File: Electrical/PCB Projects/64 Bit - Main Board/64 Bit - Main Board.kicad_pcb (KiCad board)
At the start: 4 copper layers, 200 x 100 mm, 238 parts, among them J1 61301021821, J10 M20-7920242R, J11 M20-7920242R, J12 M20-7920242R, J13 M20-7920242R, J14 1985195, J15 Conn_01x09, J16 Conn_01x09, J17 M20-7920242R, J18 M20-7920242R, J2 61301021821, J3 61301021821, J4 M20-7920242R, J5 USBC, J6 M20-7920242R, J7 PJ-102A, J8 M20-7920242R, J9 M20-7920242R, K1 JS-12N-K, K2 JS-12N-K, K3 JS-12N-K, K4 PR30-5V-450-1A-E, K5 PR30-12V-450-1A-E, P1 Conn_01x02, Q1 2N7002, Q10 XP231P0201TR-G, Q11 2N7002, Q2 XP231P0201TR-G, Q3 2N7002, Q4 2N7002, Q5 2N7002, Q6 XP231P0201TR-G, Q7 XP231P0201TR-G, Q8 2N7002, Q9 2N7002, SW1 1985195, SW2 1985195, SW3 1985195, SW4 1985195, SW5 L102011MS02Q, SW6 power_switch, U1 STM32F446RETx, U10 VEML7700-TR, U2 PCA9306, U3 DS1307+, U4 74HC3G34DC, U5 74HC3G34DC, U6 74HC3G34DC, U7 EN12-VS20AF20, U8 24LC64, U9 ESP32-C6-LCD-1.47, Y1 Crystal_GND24, Y2 32.768kHz-12.6pF, Y3 32.768kHz-12.6pF

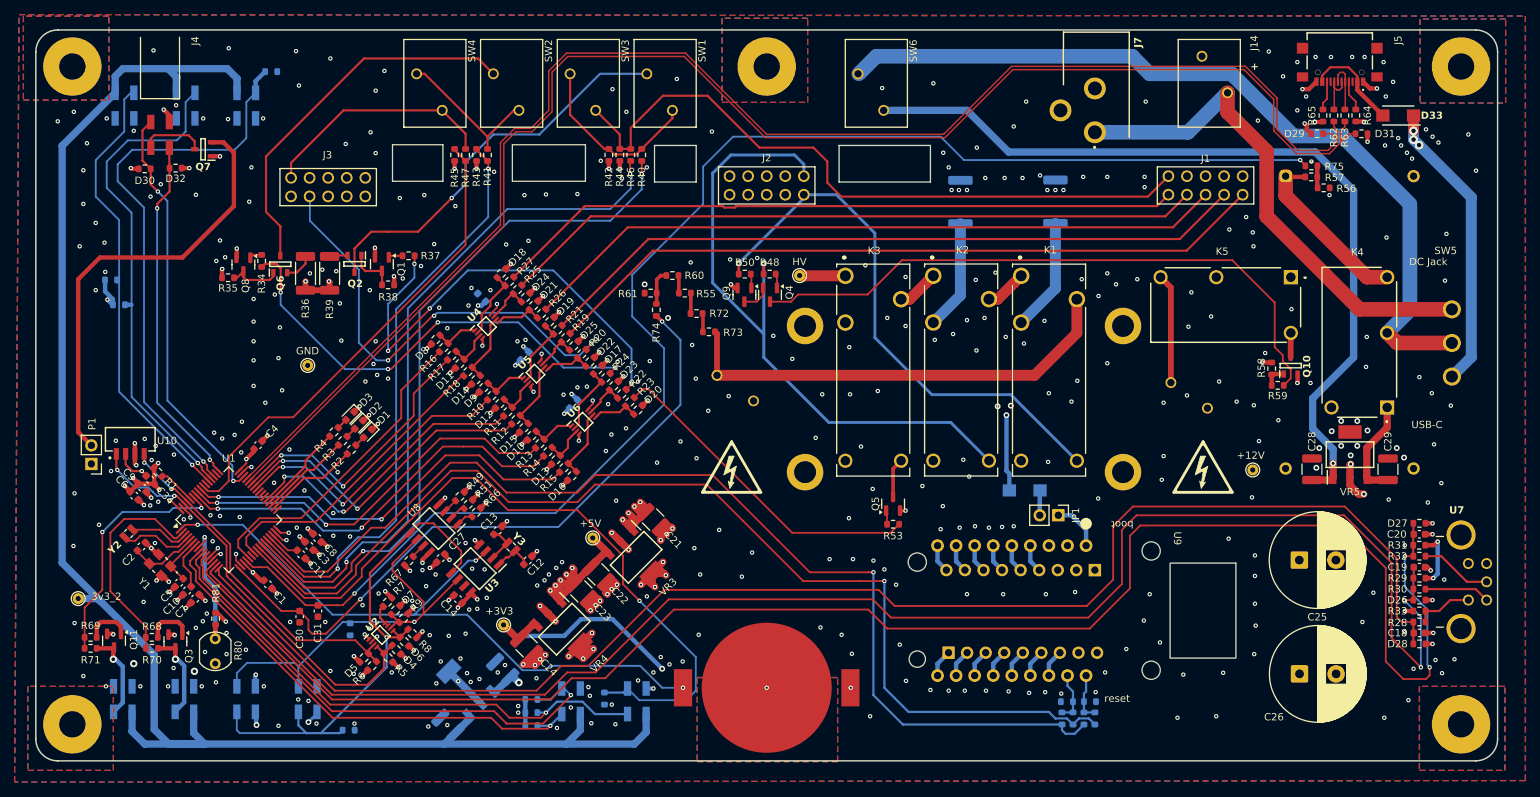
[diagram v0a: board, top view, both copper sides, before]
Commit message: near final state. Includes BOM, price, etc
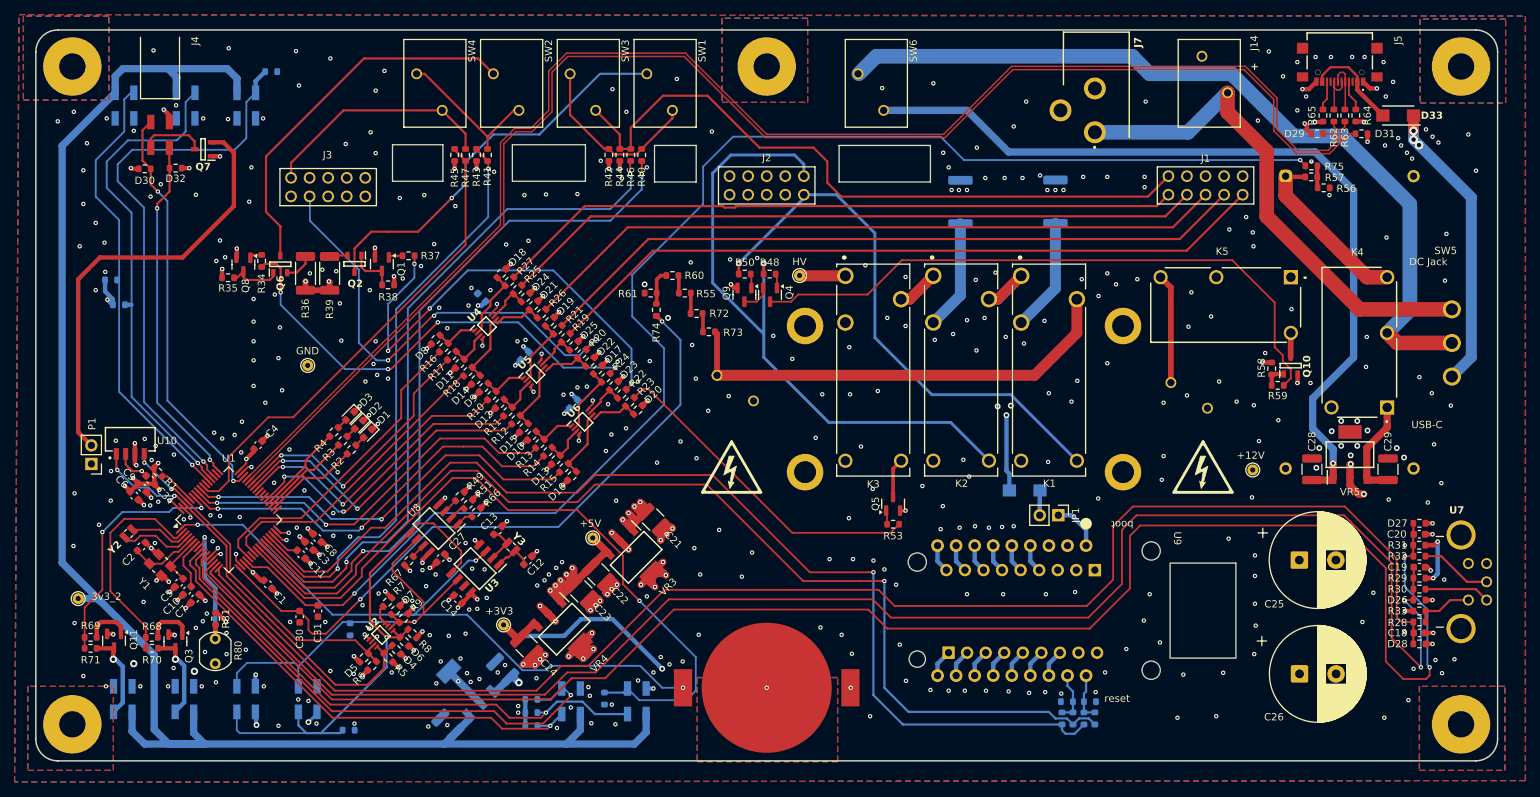
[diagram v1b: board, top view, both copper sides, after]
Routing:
- net +3V3: track 193.8 -> 192.3 mm
- net GND: vias 524 -> 525
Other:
- board text added: "'64 Bit' Nixie Tube Clock Driver Board_V1.0 Dec 2025"
- board text added: "I/0"
- board text removed: "'64 Bit' Nixie Tube Clock Driver Board_V1.0 Nov 2025"

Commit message: slight changes
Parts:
- moved REF** 1.83 mm to (66.5, 129.7)
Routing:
- net IO7: track 70.4 -> 69.8 mm

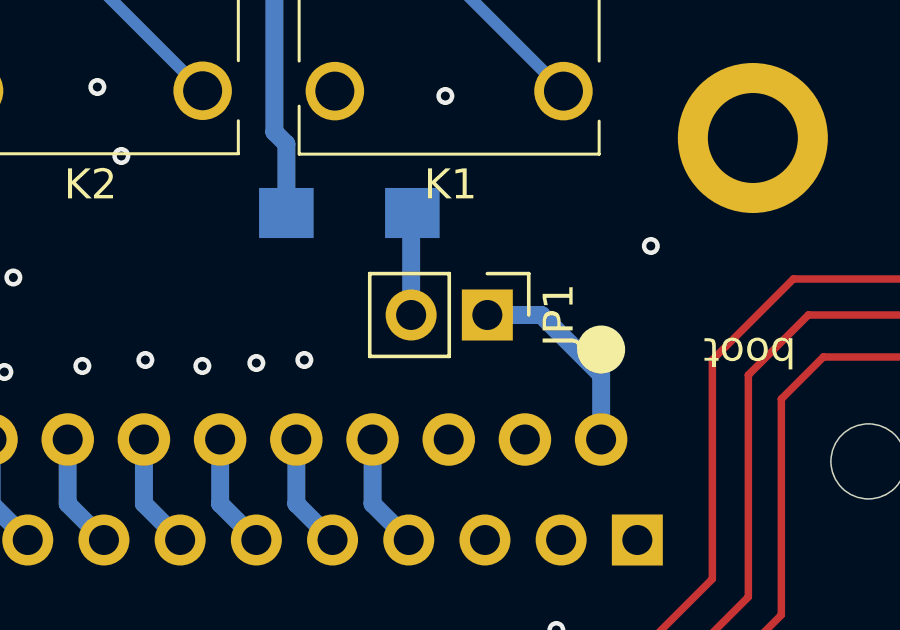
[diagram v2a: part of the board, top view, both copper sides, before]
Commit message: final. PCB outputs generated, ordering prototypes
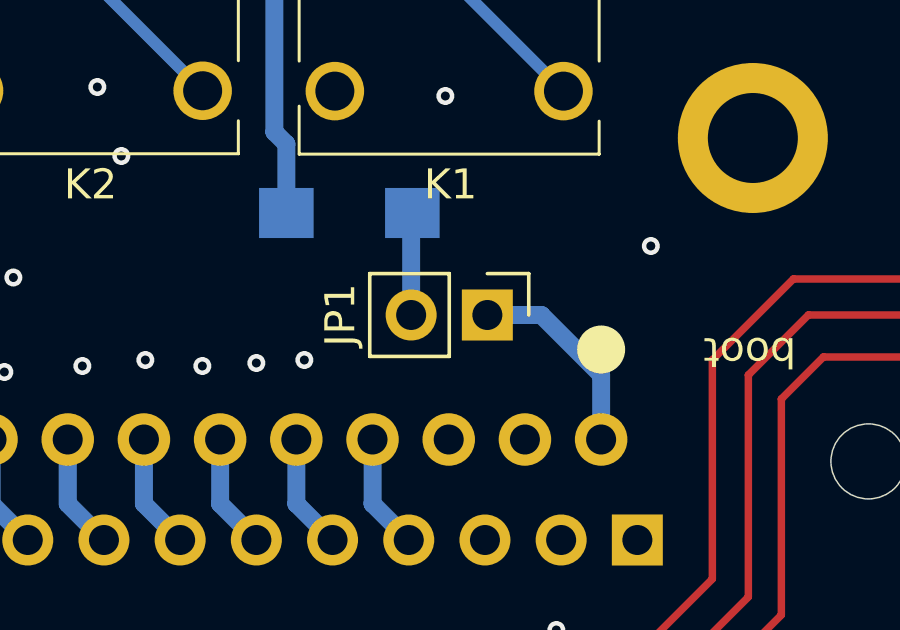
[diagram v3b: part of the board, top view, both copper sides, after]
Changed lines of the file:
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@@
 			(drillshape 0)
 			(scaleselection 1)
-			(outputdirectory "C:/Users/Kadin/Desktop/Git Projects/64-Bit/Electrical/PCB Outputs/64 Bit - Main Board/Gerbers/")
+			(outputdirectory "C:/Users/kwhit/Desktop/projects/64-Bit/Electrical/PCB Outputs/64 Bit - Main Board/Gerbers/")
 		)
 	)
@@
 		(tags "Through hole pin header THT 1x02 2.54mm single row")
 		(property "Reference" "JP1"
-			(at 0 -2.38 90)
+			(at 0 4.9 90)
 			(layer "F.SilkS")
 			(effects
@@
 	)
 	(zone
-		(net 118)
-		(net_name "Net-(SW1-B)")
+		(net 75)
+		(net_name "170V_Safety_In")
 		(layer "F.Cu")
 		(name "$teardrop_padvia$")
 		(hatch none 0.1)
-		(priority 30003)
+		(priority 30000)
 		(attr
 			(teardrop
@@
 		(polygon
 			(pts
-				(xy 124.95 47.985589) (xy 125.25 47.985589) (xy 125.723602 46.916678) (xy 125.1 46.499) (xy 124.476398 46.916678)
+				(xy 145.6 86.264411) (xy 144.8 86.264411) (xy 144.464411 87.603682) (xy 145.2 87.751) (xy 145.935589 87.603682)
 			)
 		)
 	)
 	(zone
-		(net 94)
-		(net_name "Net-(Q6-D)")
+		(net 121)
+		(net_name "Net-(SW2-B)")
 		(layer "F.Cu")
 		(name "$teardrop_padvia$")
 		(hatch none 0.1)
-		(priority 30002)
+		(priority 30001)
 		(attr
 			(teardrop
@@
 		(polygon
 			(pts
-				(xy 113.655596 45.343464) (xy 113.443464 45.555596) (xy 113.864411 46.646318) (xy 114.600707 46.500707)
-				(xy 114.746318 45.764411)
+				(xy 105.366586 46.878718) (xy 105.578718 46.666586) (xy 104.516678 45.876398) (xy 104.099293 46.499293)
+				(xy 104.246318 47.235589)
+			)
+		)
+	)
+	(zone
+		(net 118)
+		(net_name "Net-(SW1-B)")
+		(layer "F.Cu")
+		(name "$teardrop_padvia$")
+		(hatch none 0.1)
+		(priority 30003)
+		(attr
+			(teardrop
+				(type padvia)
+			)
+		)
+		(connect_pads yes
+			(clearance 0)
+		)
+		(min_thickness 0.0254)
+		(filled_areas_thickness no)
+		(fill yes
+			(thermal_gap 0.5)
+			(thermal_bridge_width 0.5)
+			(island_removal_mode 1)
+			(island_area_min 10)
+		)
+		(polygon
+			(pts
+				(xy 124.95 47.985589) (xy 125.25 47.985589) (xy 125.723602 46.916678) (xy 125.1 46.499) (xy 124.476398 46.916678)
 			)
 		)
@@
 	)
 	(zone
-		(net 75)
-		(net_name "170V_Safety_In")
-		(layer "F.Cu")
-		(name "$teardrop_padvia$")
-		(hatch none 0.1)
-		(priority 30000)
-		(attr
-			(teardrop
-				(type padvia)
-			)
-		)
-		(connect_pads yes
-			(clearance 0)
-		)
-		(min_thickness 0.0254)
-		(filled_areas_thickness no)
-		(fill yes
-			(thermal_gap 0.5)
-			(thermal_bridge_width 0.5)
-			(island_removal_mode 1)
-			(island_area_min 10)
-		)
-		(polygon
-			(pts
-				(xy 145.6 86.264411) (xy 144.8 86.264411) (xy 144.464411 87.603682) (xy 145.2 87.751) (xy 145.935589 87.603682)
-			)
-		)
-	)
-	(zone
-		(net 121)
-		(net_name "Net-(SW2-B)")
+		(net 94)
+		(net_name "Net-(Q6-D)")
 		(layer "F.Cu")
 		(name "$teardrop_padvia$")
 		(hatch none 0.1)
-		(priority 30001)
+		(priority 30002)
 		(attr
 			(teardrop
@@
 		(polygon
 			(pts
-				(xy 105.366586 46.878718) (xy 105.578718 46.666586) (xy 104.516678 45.876398) (xy 104.099293 46.499293)
-				(xy 104.246318 47.235589)
+				(xy 113.655596 45.343464) (xy 113.443464 45.555596) (xy 113.864411 46.646318) (xy 114.600707 46.500707)
+				(xy 114.746318 45.764411)
 			)
 		)
@@
 		(net 2)
 		(net_name "GND")
-		(layers "F.Cu" "B.Cu")
+		(layers "F.Cu" "B.Cu" "In1.Cu")
 		(hatch edge 0.5)
-		(priority 1)
-		(connect_pads yes
-			(clearance 0.5)
+		(connect_pads
+			(clearance 0.8)
 		)
 		(min_thickness 0.25)
@@
 		(polygon
 			(pts
-				(xy 157.6 50.4) (xy 157.6 38.9) (xy 145.9 38.9) (xy 145.9 50.4)
+				(xy 49.7 38.4) (xy 255.8 38.6) (xy 255.8 143.2) (xy 49.1 143.4)
 			)
 		)
@@
 		(layers "F.Cu" "B.Cu" "In1.Cu")
 		(hatch edge 0.5)
-		(connect_pads
-			(clearance 0.8)
+		(priority 1)
+		(connect_pads yes
+			(clearance 0.5)
 		)
 		(min_thickness 0.25)
@@
 		(polygon
 			(pts
-				(xy 49.7 38.4) (xy 255.8 38.6) (xy 255.8 143.2) (xy 49.1 143.4)
+				(xy 253.1 50.5) (xy 253.1 39) (xy 241.4 39) (xy 241.4 50.5)
 			)
 		)
@@
 		(polygon
 			(pts
-				(xy 253.1 50.5) (xy 253.1 39) (xy 241.4 39) (xy 241.4 50.5)
+				(xy 157.6 50.4) (xy 157.6 38.9) (xy 145.9 38.9) (xy 145.9 50.4)
 			)
 		)
